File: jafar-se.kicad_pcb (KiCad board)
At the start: 2 copper layers, 33 x 41 mm, 16 parts, among them J1 XBOX LPC, J2 JTAG, J3 D0, J4 PLCC-32 Socket, U1 LC4032V-75TN44I

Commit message: Minor fixes
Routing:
- net /TMS: track 8.72 -> 7.74 mm
- net /~{XLRESET}: track 39.8 -> 40.5 mm
- net GND: vias 55 -> 53

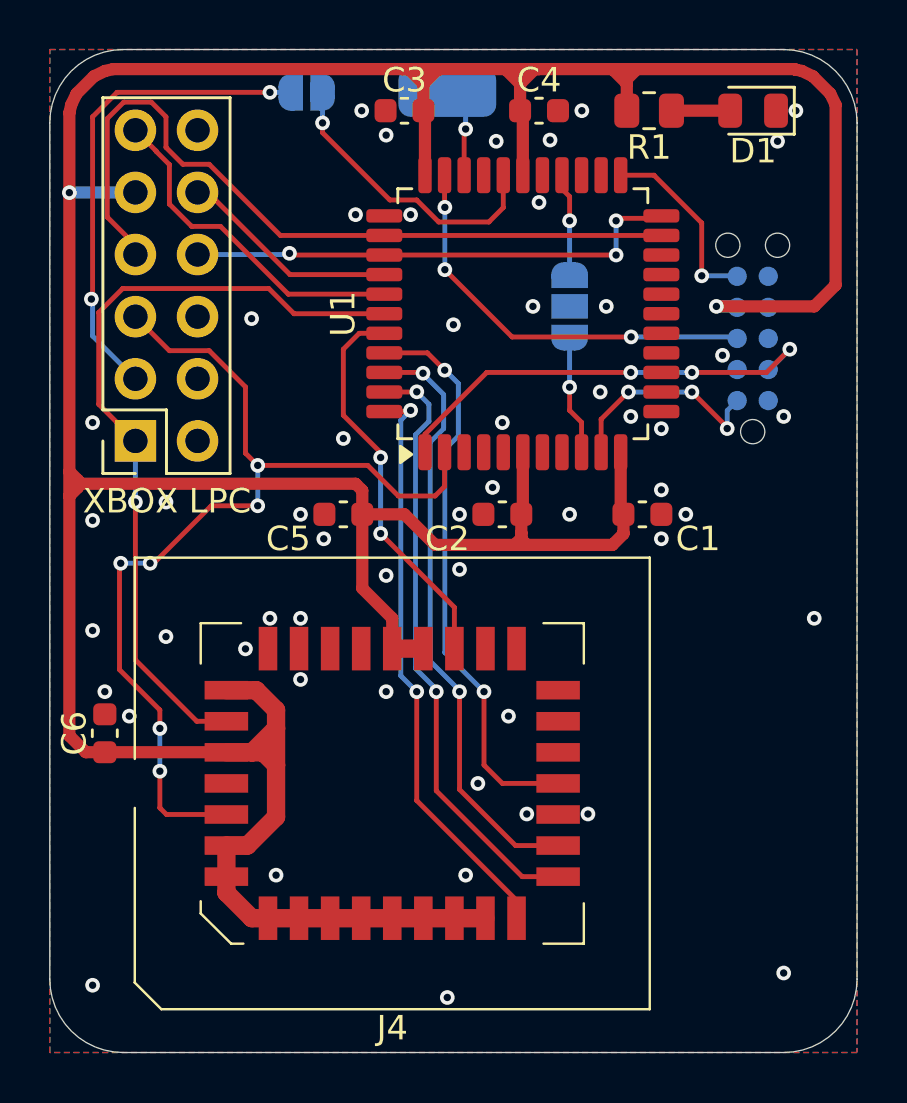
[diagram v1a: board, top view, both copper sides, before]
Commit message: Increase trace widths to .3mm
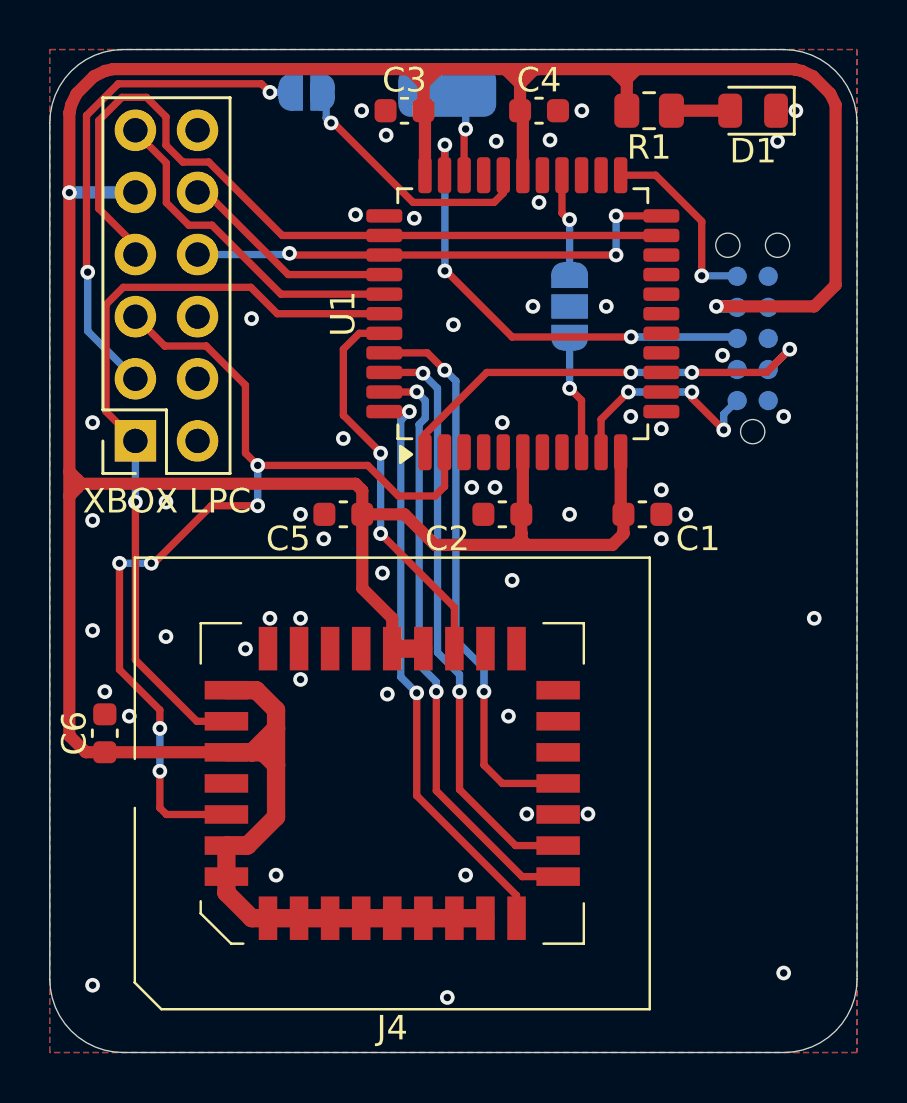
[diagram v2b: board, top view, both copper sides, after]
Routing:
- net /TDO: track 17.0 -> 19.5 mm
- net /XLFRAME_L1: track 12.2 -> 10.7 mm
- net /~{XLFRAME}: track 20.0 -> 20.6 mm
- net /XLAD3: track 32.0 -> 32.5 mm
- net /BT: track 4.19 -> 3.66 mm
- net /FLAD2: track 24.7 -> 24.2 mm
- net GND: vias 53 -> 51

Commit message: WIP change JTAG header
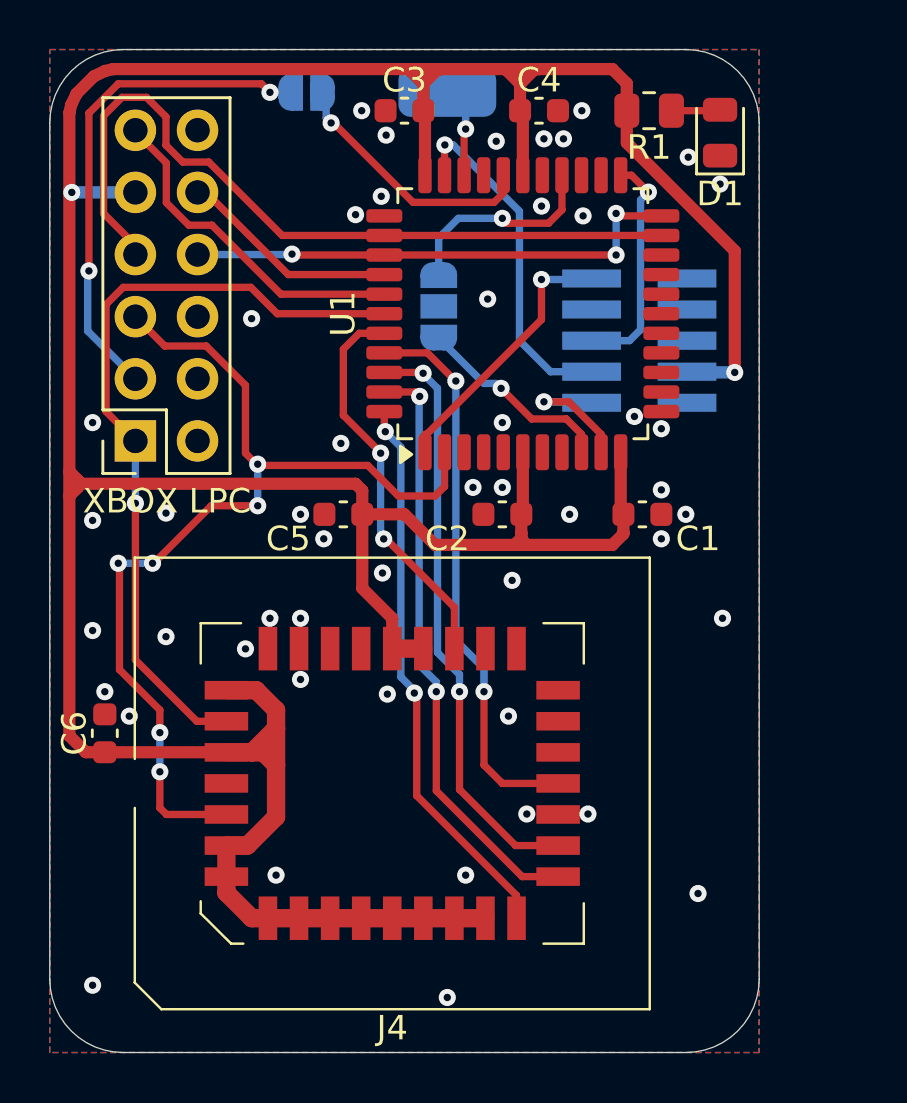
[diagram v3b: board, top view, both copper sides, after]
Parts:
- J2: footprint Connector:Tag-Connect_TC2050-IDC-NL_2x05_P1.27mm_Vertical -> Connector_PinHeader_1.27mm:PinHeader_2x05_P1.27mm_Vertical_SMD
- moved JP1 5.35 mm to (135.9, 57.5)
- moved J2 4.63 mm to (144.1, 58.9), turned to 0 degrees
- moved D1 1.62 mm to (147.4, 50.4), turned to 90 degrees
- moved G*** 0.50 mm to (136.8, 69.8)
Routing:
- net +3V3: track 163.2 -> 153.6 mm
- net /TDI: track 18.3 -> 11.8 mm, vias 3 -> 1
- net /TDO: track 19.5 -> 14.2 mm, vias 3 -> 1
- net /BT: track 3.66 -> 8.59 mm
- net /TCK: track 9.04 -> 5.59 mm, vias 3 -> 1
- net /H0: track 4.88 -> 8.22 mm
- net /TMS: track 7.78 -> 9.36 mm
- net /FLAD0: track 23.8 -> 22.9 mm
- net GND: vias 51 -> 49
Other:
- board size 33 x 41 mm -> 29 x 41 mm

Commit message: Revert "WIP change JTAG header"
This reverts commit d418005aa1de2dce9ff1cfefd18ff509fc34da6a.
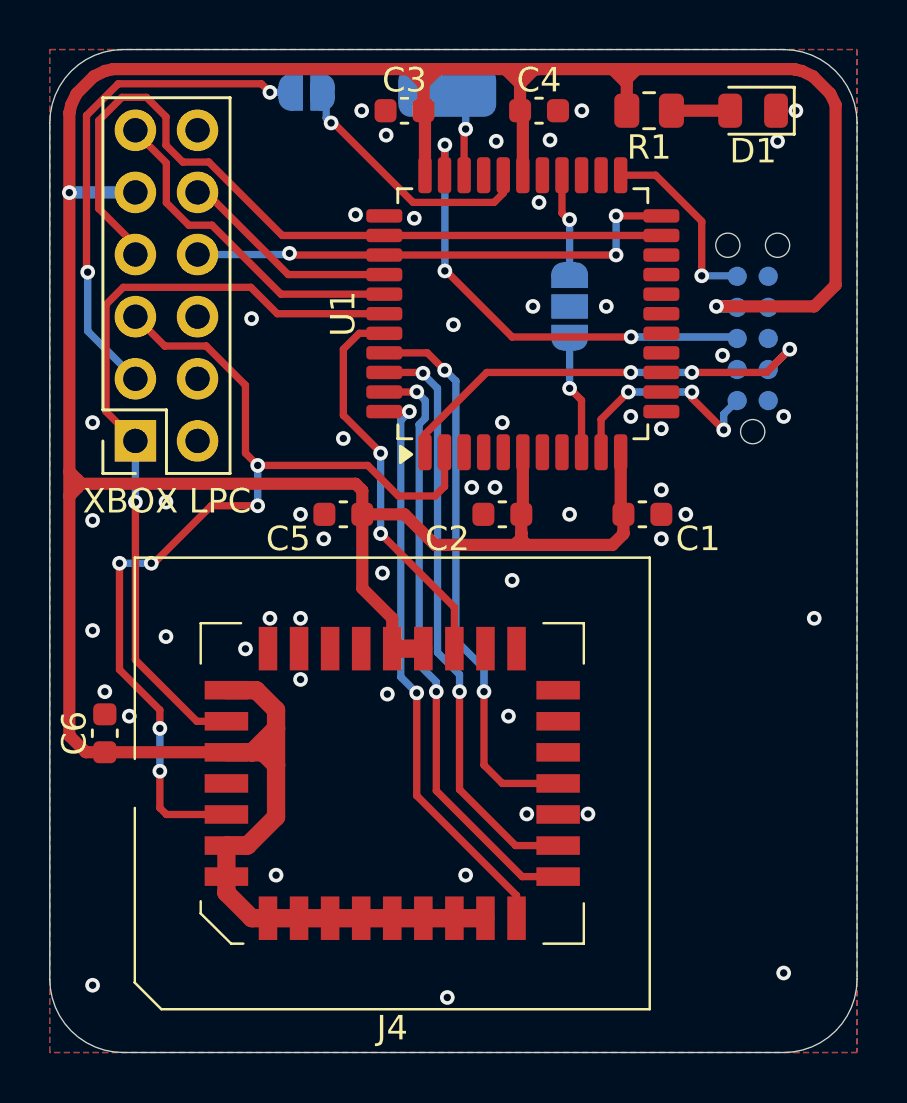
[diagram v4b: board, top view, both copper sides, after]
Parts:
- J2: footprint Connector_PinHeader_1.27mm:PinHeader_2x05_P1.27mm_Vertical_SMD -> Connector:Tag-Connect_TC2050-IDC-NL_2x05_P1.27mm_Vertical
- moved JP1 5.35 mm to (141.2, 57.5)
- moved J2 4.63 mm to (148.7, 58.8), turned to 90 degrees
- moved D1 1.62 mm to (148.8, 49.5), turned to 180 degrees
- moved G*** 0.50 mm to (136.8, 69.2)
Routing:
- net +3V3: track 153.6 -> 163.2 mm
- net /TDI: track 11.8 -> 18.3 mm, vias 1 -> 3
- net /TDO: track 14.2 -> 19.5 mm, vias 1 -> 3
- net /BT: track 8.59 -> 3.66 mm
- net /TCK: track 5.59 -> 9.04 mm, vias 1 -> 3
- net /H0: track 8.22 -> 4.88 mm
- net /TMS: track 9.36 -> 7.78 mm
- net /FLAD0: track 22.9 -> 23.8 mm
- net GND: vias 49 -> 51
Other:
- board size 29 x 41 mm -> 33 x 41 mm

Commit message: Fix via sizes
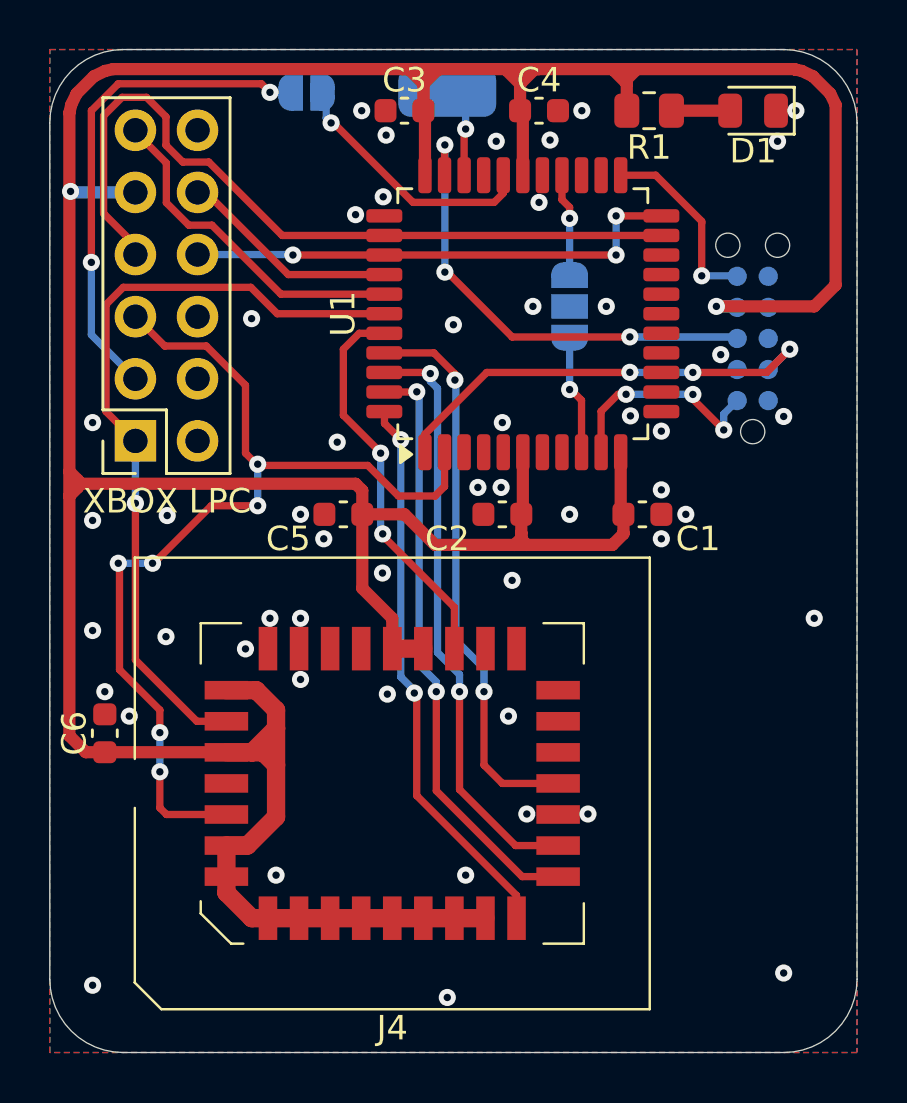
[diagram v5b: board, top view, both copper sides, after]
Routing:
- net /FLAD0: track 23.8 -> 22.9 mm
